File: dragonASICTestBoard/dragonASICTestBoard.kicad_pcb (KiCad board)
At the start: 2 copper layers, 0 parts

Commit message: Add schematic and layout to dragonASICTestBoard
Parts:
- added P1: CONN_01X20, Pin_Headers:Pin_Header_Straight_1x20_Pitch2.54mm, F.Cu at (128.0, 80.3)
- added P2, P3, P4: CONN_01X20, Pin_Headers:Pin_Header_Straight_1x20_Pitch2.54mm, F.Cu at (117.9, 80.3)
- added U1: die80, dragonASICTestBoard:die80, F.Cu at (148.5, 105.0)

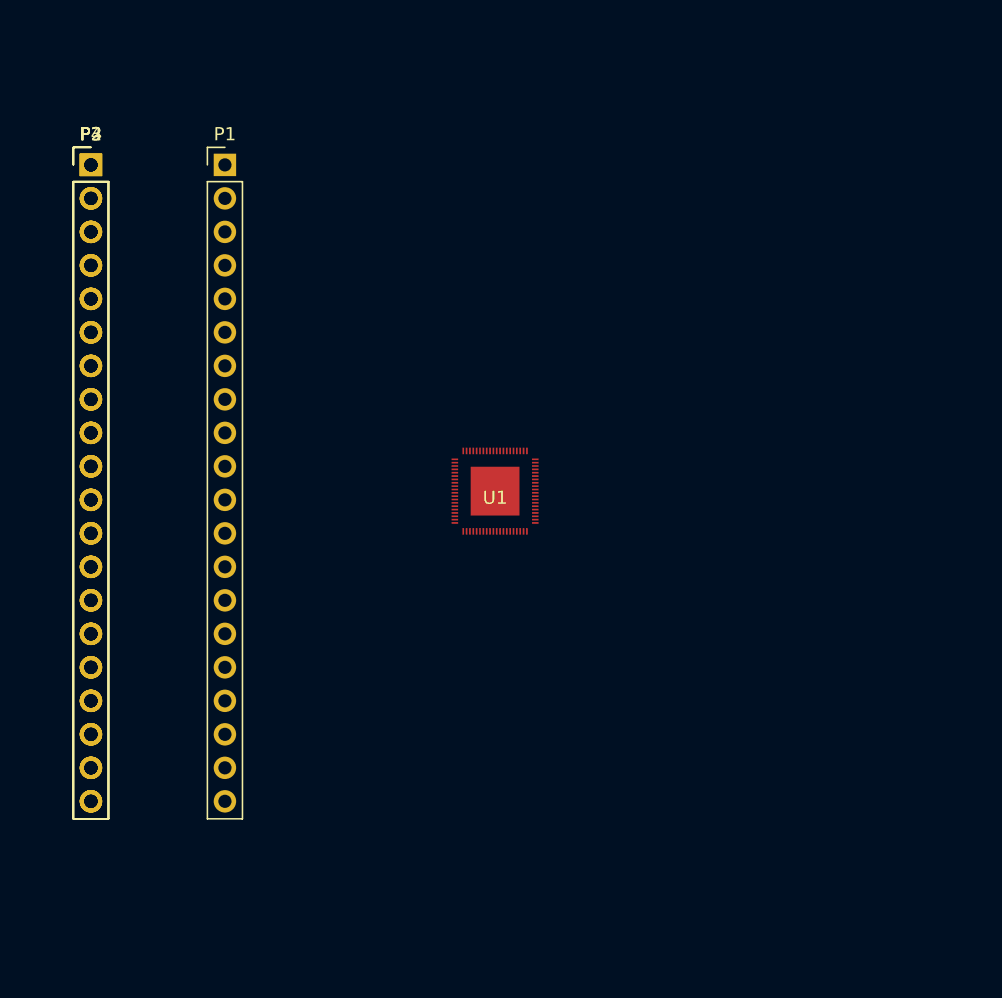
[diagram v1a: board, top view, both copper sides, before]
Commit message: Add PCB layout to dragonASICTestBoard
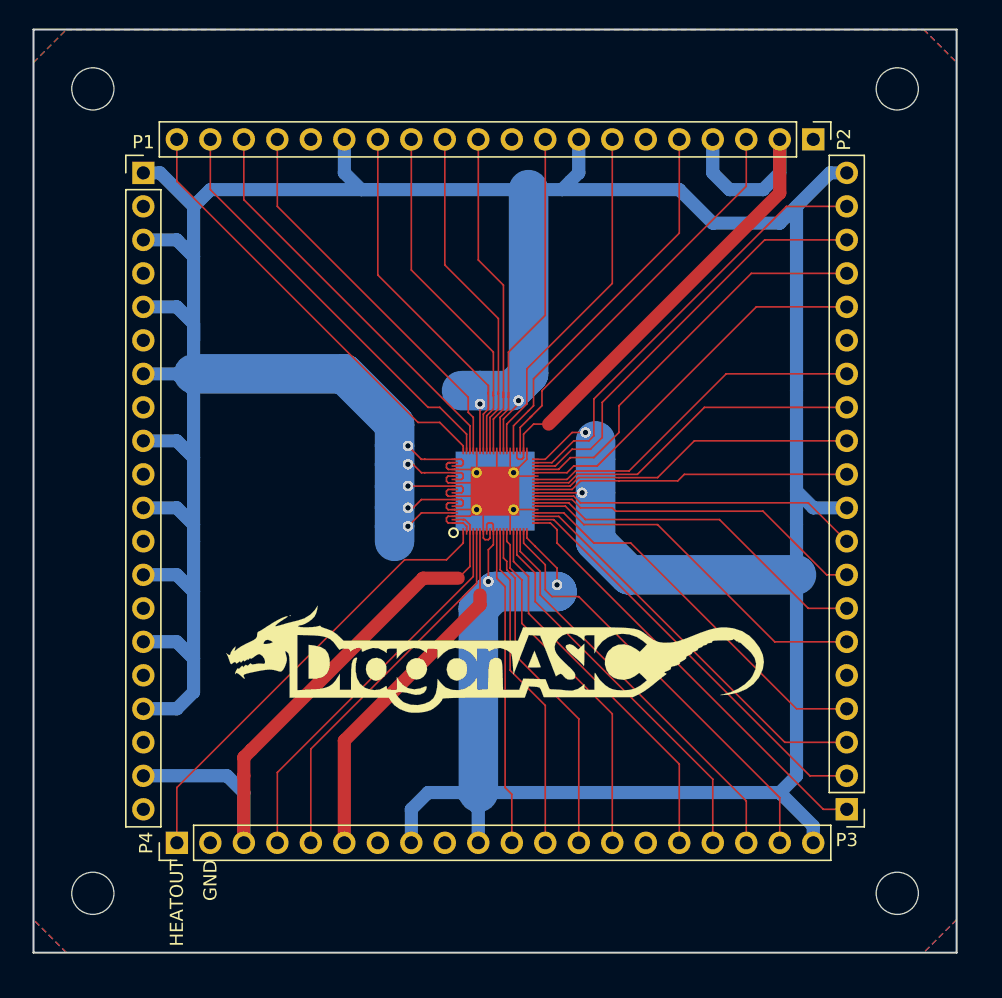
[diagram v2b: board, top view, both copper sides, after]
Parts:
- added ?: MountingHole_3.2mm_M3, Mounting_Holes:MountingHole_3.2mm_M3, F.Cu at (179.0, 74.5)
- added ?: MountingHole_3.2mm_M3, Mounting_Holes:MountingHole_3.2mm_M3, F.Cu at (179.0, 135.5)
- added ?: MountingHole_3.2mm_M3, Mounting_Holes:MountingHole_3.2mm_M3, F.Cu at (118.0, 135.5)
- added ?: MountingHole_3.2mm_M3, Mounting_Holes:MountingHole_3.2mm_M3, F.Cu at (118.0, 74.5)
- added G***: LOGO, dragonASICTestBoard:logo, F.Cu at (148.5, 117.7)
- moved P3 75.3 mm to (175.2, 129.1), turned to 180 degrees
- moved P2 54.8 mm to (172.6, 78.3), turned to 270 degrees
- moved P4 51.8 mm to (124.4, 131.7), turned to 90 degrees
- moved P1 6.22 mm to (121.8, 80.9)
- renumbered U1 to ?
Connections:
- ? pad 0: (no net) -> GND
- ? pad 1: (no net) -> Net-(P4-Pad1)
- ? pad 10: (no net) -> /VDD
- ? pad 11: (no net) -> Net-(P4-Pad11)
- ? pad 12: (no net) -> Net-(P4-Pad12)
- ? pad 13: (no net) -> Net-(P4-Pad13)
- ? pad 14: (no net) -> Net-(P4-Pad14)
- ? pad 15: (no net) -> GND
- ? pad 16: (no net) -> Net-(P4-Pad16)
- ? pad 17: (no net) -> Net-(P4-Pad17)
- ? pad 18: (no net) -> Net-(P4-Pad18)
- ? pad 19: (no net) -> Net-(P4-Pad19)
- ? pad 2: (no net) -> GND
- ? pad 20: (no net) -> /VDD
- ? pad 21: (no net) -> Net-(P3-Pad1)
- ? pad 22: (no net) -> Net-(P3-Pad2)
- ? pad 23: (no net) -> Net-(P3-Pad3)
- ? pad 24: (no net) -> Net-(P3-Pad4)
- ? pad 25: (no net) -> GND
- ? pad 26: (no net) -> Net-(P3-Pad6)
- ? pad 27: (no net) -> Net-(P3-Pad7)
- ? pad 28: (no net) -> Net-(P3-Pad8)
- ? pad 29: (no net) -> Net-(P3-Pad9)
- ? pad 3: (no net) -> /VDDHEAT
- ? pad 30: (no net) -> /VDD
- ? pad 31: (no net) -> Net-(P3-Pad11)
- ? pad 32: (no net) -> Net-(P3-Pad12)
- ? pad 33: (no net) -> Net-(P3-Pad13)
- ? pad 34: (no net) -> Net-(P3-Pad14)
- ? pad 35: (no net) -> GND
- ? pad 36: (no net) -> Net-(P3-Pad16)
- ? pad 37: (no net) -> Net-(P3-Pad17)
- ? pad 38: (no net) -> Net-(P3-Pad18)
- ? pad 39: (no net) -> Net-(P3-Pad19)
- ? pad 4: (no net) -> Net-(P4-Pad4)
- ? pad 40: (no net) -> /VDD
- ? pad 41: (no net) -> GND
- ? pad 42: (no net) -> /VDDVCO
- ? pad 43: (no net) -> Net-(P2-Pad3)
- ? pad 44: (no net) -> /VDDVCO
- ? pad 45: (no net) -> Net-(P2-Pad5)
- ? pad 46: (no net) -> GND
- ? pad 47: (no net) -> Net-(P2-Pad7)
- ? pad 48: (no net) -> /VDD
- ? pad 49: (no net) -> Net-(P2-Pad9)
- ? pad 5: (no net) -> Net-(P4-Pad5)
- ? pad 50: (no net) -> GND
- ? pad 51: (no net) -> Net-(P2-Pad11)
- ? pad 52: (no net) -> Net-(P2-Pad12)
- ? pad 53: (no net) -> Net-(P2-Pad13)
- ? pad 54: (no net) -> Net-(P2-Pad14)
- ? pad 55: (no net) -> /VDD
- ? pad 56: (no net) -> GND
- ? pad 57: (no net) -> Net-(P2-Pad17)
- ? pad 58: (no net) -> Net-(P2-Pad18)
- ? pad 59: (no net) -> Net-(P2-Pad19)
- ? pad 6: (no net) -> /VDDPHOTO
- ? pad 60: (no net) -> Net-(P2-Pad20)
- ? pad 61: Net-(P1-Pad1) -> /VDD
- ? pad 62: Net-(P1-Pad2) -> GND
- ? pad 63: Net-(P1-Pad3) -> /VDD
- ? pad 64: Net-(P1-Pad4) -> GND
- ? pad 65: Net-(P1-Pad5) -> /VDD
- ? pad 66: Net-(P1-Pad6) -> GND
- ? pad 67: Net-(P1-Pad7) -> /VDD
- ? pad 68: Net-(P1-Pad8) -> GND
- ? pad 69: Net-(P1-Pad9) -> /VDD
- ? pad 7: (no net) -> GND
- ? pad 70: Net-(P1-Pad10) -> GND
- ? pad 71: Net-(P1-Pad11) -> /VDD
- ? pad 72: Net-(P1-Pad12) -> GND
- ? pad 73: Net-(P1-Pad13) -> /VDD
- ? pad 74: Net-(P1-Pad14) -> GND
- ? pad 75: Net-(P1-Pad15) -> /VDD
- ? pad 76: Net-(P1-Pad16) -> GND
- ? pad 77: Net-(P1-Pad17) -> /VDD
- ? pad 78: Net-(P1-Pad18) -> GND
- ? pad 79: Net-(P1-Pad19) -> /VDDHEAT
- ? pad 8: (no net) -> /VDD
- ? pad 80: Net-(P1-Pad20) -> GND
- ? pad 9: (no net) -> GND
- P1 pad 1: Net-(P1-Pad1) -> /VDD
- P1 pad 10: Net-(P1-Pad10) -> GND
- P1 pad 11: Net-(P1-Pad11) -> /VDD
- P1 pad 12: Net-(P1-Pad12) -> GND
- P1 pad 13: Net-(P1-Pad13) -> /VDD
- P1 pad 14: Net-(P1-Pad14) -> GND
- P1 pad 15: Net-(P1-Pad15) -> /VDD
- P1 pad 16: Net-(P1-Pad16) -> GND
- P1 pad 17: Net-(P1-Pad17) -> /VDD
- P1 pad 18: Net-(P1-Pad18) -> GND
- P1 pad 19: Net-(P1-Pad19) -> /VDDHEAT
- P1 pad 2: Net-(P1-Pad2) -> GND
- P1 pad 20: Net-(P1-Pad20) -> GND
- P1 pad 3: Net-(P1-Pad3) -> /VDD
- P1 pad 4: Net-(P1-Pad4) -> GND
- P1 pad 5: Net-(P1-Pad5) -> /VDD
- P1 pad 6: Net-(P1-Pad6) -> GND
- P1 pad 7: Net-(P1-Pad7) -> /VDD
- P1 pad 8: Net-(P1-Pad8) -> GND
- P1 pad 9: Net-(P1-Pad9) -> /VDD
- P2 pad 1: (no net) -> GND
- P2 pad 10: (no net) -> GND
- P2 pad 11: (no net) -> Net-(P2-Pad11)
- P2 pad 12: (no net) -> Net-(P2-Pad12)
- P2 pad 13: (no net) -> Net-(P2-Pad13)
- P2 pad 14: (no net) -> Net-(P2-Pad14)
- P2 pad 15: (no net) -> /VDD
- P2 pad 16: (no net) -> GND
- P2 pad 17: (no net) -> Net-(P2-Pad17)
- P2 pad 18: (no net) -> Net-(P2-Pad18)
- P2 pad 19: (no net) -> Net-(P2-Pad19)
- P2 pad 2: (no net) -> /VDDVCO
- P2 pad 20: (no net) -> Net-(P2-Pad20)
- P2 pad 3: (no net) -> Net-(P2-Pad3)
- P2 pad 4: (no net) -> /VDDVCO
- P2 pad 5: (no net) -> Net-(P2-Pad5)
- P2 pad 6: (no net) -> GND
- P2 pad 7: (no net) -> Net-(P2-Pad7)
- P2 pad 8: (no net) -> /VDD
- P2 pad 9: (no net) -> Net-(P2-Pad9)
- P3 pad 1: (no net) -> Net-(P3-Pad1)
- P3 pad 10: (no net) -> /VDD
- P3 pad 11: (no net) -> Net-(P3-Pad11)
- P3 pad 12: (no net) -> Net-(P3-Pad12)
- P3 pad 13: (no net) -> Net-(P3-Pad13)
- P3 pad 14: (no net) -> Net-(P3-Pad14)
- P3 pad 15: (no net) -> GND
- P3 pad 16: (no net) -> Net-(P3-Pad16)
- P3 pad 17: (no net) -> Net-(P3-Pad17)
- P3 pad 18: (no net) -> Net-(P3-Pad18)
- P3 pad 19: (no net) -> Net-(P3-Pad19)
- P3 pad 2: (no net) -> Net-(P3-Pad2)
- P3 pad 20: (no net) -> /VDD
- P3 pad 3: (no net) -> Net-(P3-Pad3)
- P3 pad 4: (no net) -> Net-(P3-Pad4)
- P3 pad 5: (no net) -> GND
- P3 pad 6: (no net) -> Net-(P3-Pad6)
- P3 pad 7: (no net) -> Net-(P3-Pad7)
- P3 pad 8: (no net) -> Net-(P3-Pad8)
- P3 pad 9: (no net) -> Net-(P3-Pad9)
- P4 pad 1: (no net) -> Net-(P4-Pad1)
- P4 pad 10: (no net) -> /VDD
- P4 pad 11: (no net) -> Net-(P4-Pad11)
- P4 pad 12: (no net) -> Net-(P4-Pad12)
- P4 pad 13: (no net) -> Net-(P4-Pad13)
- P4 pad 14: (no net) -> Net-(P4-Pad14)
- P4 pad 15: (no net) -> GND
- P4 pad 16: (no net) -> Net-(P4-Pad16)
- P4 pad 17: (no net) -> Net-(P4-Pad17)
- P4 pad 18: (no net) -> Net-(P4-Pad18)
- P4 pad 19: (no net) -> Net-(P4-Pad19)
- P4 pad 2: (no net) -> GND
- P4 pad 20: (no net) -> /VDD
- P4 pad 3: (no net) -> /VDDHEAT
- P4 pad 4: (no net) -> Net-(P4-Pad4)
- P4 pad 5: (no net) -> Net-(P4-Pad5)
- P4 pad 6: (no net) -> /VDDPHOTO
- P4 pad 7: (no net) -> GND
- P4 pad 8: (no net) -> /VDD
- P4 pad 9: (no net) -> GND
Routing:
- net /VDD: track 0.00 -> 413.8 mm, vias 0 -> 11
- net /VDDHEAT: track 0.00 -> 46.1 mm
- net GND: track 0.00 -> 45.9 mm
- net /VDDVCO: track 0.00 -> 45.2 mm
- net Net-(P4-Pad1): track 0.00 -> 34.5 mm
- net Net-(P2-Pad20): track 0.00 -> 33.6 mm
- net Net-(P3-Pad19): track 0.00 -> 33.3 mm
- net Net-(P3-Pad1): track 0.00 -> 33.2 mm
- net Net-(P4-Pad19): track 0.00 -> 32.9 mm
- net Net-(P3-Pad18): track 0.00 -> 32.3 mm
- net Net-(P2-Pad19): track 0.00 -> 32.2 mm
- net Net-(P3-Pad2): track 0.00 -> 31.7 mm
- net Net-(P3-Pad17): track 0.00 -> 31.0 mm
- net Net-(P2-Pad3): track 0.00 -> 30.9 mm
- net Net-(P2-Pad18): track 0.00 -> 30.7 mm
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- added copper zone on B.Cu, net GND
- added copper zone on F.Cu, net GND
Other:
- board outline added: 70 x 70 mm
- net class Default: clearance 0.2 -> 0.12
- rule pad_to_mask_clearance: 0.2 -> 0
- rule trace_clearance: 0.2 -> 0.12
- rule trace_min: 0.2 -> 0.127
- board text added: "GND"
- board text added: "HEATOUT"

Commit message: Fix PCB layout of dragonASICTestBoard
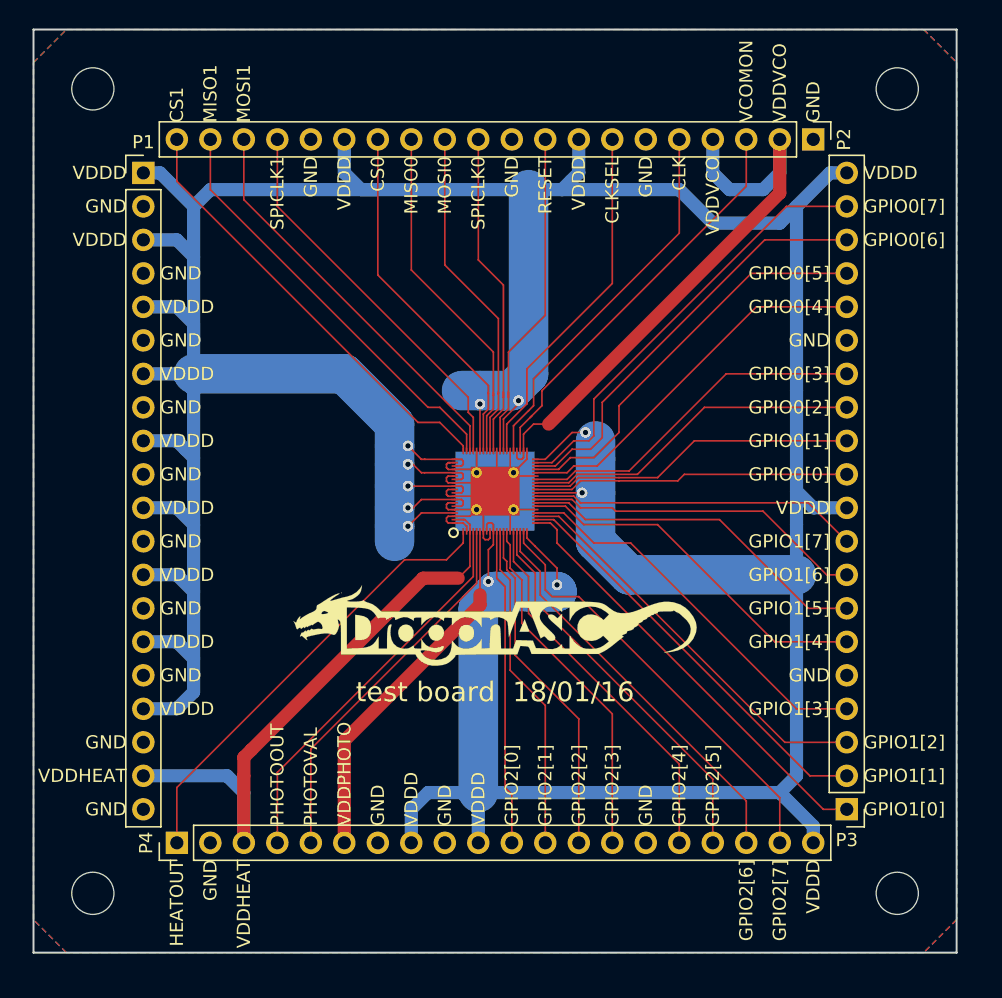
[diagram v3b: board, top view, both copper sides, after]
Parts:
- moved G*** 2.54 mm to (148.5, 115.2)
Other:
- board text added: "CLK"
- board text added: "CLKSEL"
- board text added: "CS0"
- board text added: "CS1"
- board text added: "GPIO0[0]"
- board text added: "GPIO0[1]"
- board text added: "GPIO0[2]"
- board text added: "GPIO0[3]"
- board text added: "GPIO0[4]"
- board text added: "GPIO0[5]"
- board text added: "GPIO0[6]"
- board text added: "GPIO0[7]"
- board text added: "GPIO1[0]"
- board text added: "GPIO1[1]"
- board text added: "GPIO1[2]"
- board text added: "GPIO1[3]"
- board text added: "GPIO1[4]"
- board text added: "GPIO1[5]"
- board text added: "GPIO1[6]"
- board text added: "GPIO1[7]"
- board text added: "GPIO2[0]"
- board text added: "GPIO2[1]"
- board text added: "GPIO2[2]"
- board text added: "GPIO2[3]"
- board text added: "GPIO2[4]"
- board text added: "GPIO2[5]"
- board text added: "GPIO2[6]"
- board text added: "GPIO2[7]"
- board text added: "MISO0"
- board text added: "MISO1"
- board text added: "MOSI0"
- board text added: "MOSI1"
- board text added: "PHOTOOUT"
- board text added: "PHOTOVAL"
- board text added: "RESET"
- board text added: "SPICLK0"
- board text added: "SPICLK1"
- board text added: "VCOMON"
- board text added: "VDDD"
- board text added: "VDDHEAT"
- board text added: "VDDPHOTO"
- board text added: "VDDVCO"
- board text added: "test board 18/01/16"
